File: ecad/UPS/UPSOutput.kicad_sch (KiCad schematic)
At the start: 28 parts, among them J3 USB_C_Receptacle_USB2.0_16P, Q3 IRLR7843TRPBF, SW3 SW_DPDT_x2, U2 MPQ5031GRE-0001-AEC1-P, U3 L78L05_SOT89

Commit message: Output section of PCB
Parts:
- C10, C11, C12, C60: footprint (none) -> Capacitor_SMD:C_0805_2012Metric_Pad1.18x1.45mm_HandSolder
- C5, C59, C6, C7, C8, C9: footprint (none) -> Capacitor_SMD:C_0603_1608Metric_Pad1.08x0.95mm_HandSolder
- R6, R7: footprint (none) -> Resistor_SMD:R_1206_3216Metric_Pad1.30x1.75mm_HandSolder
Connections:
- net CC1: now also D1.1 (K), J3.A5 (CC1), R7.1; no longer D2.1 (K), J3.B5 (CC2), R6.2
- net CC2: now also D2.1 (K), J3.B5 (CC2), R6.2; no longer D1.1 (K), J3.A5 (CC1), R7.1
- net VBUS renamed VBUS_out
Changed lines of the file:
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@@
 		)
 	)
-	(label "CC2"
-		(at 217.17 64.77 0)
+	(label "D+"
+		(at 217.17 52.07 0)
 		(effects
 			(font
@@
 		)
 	)
-	(label "CC1"
-		(at 217.17 62.23 0)
+	(label "VBUS_in"
+		(at 39.37 102.87 0)
 		(effects
 			(font
@@
 		)
 	)
-	(label "D+"
-		(at 217.17 52.07 0)
+	(label "SCL"
+		(at 29.21 62.23 0)
 		(effects
 			(font
@@
 		)
 	)
-	(label "SCL"
-		(at 29.21 62.23 0)
+	(label "D-"
+		(at 217.17 54.61 0)
 		(effects
 			(font
@@
 		)
 	)
-	(label "D-"
-		(at 217.17 54.61 0)
+	(label "VBUS_out"
+		(at 217.17 102.87 0)
 		(effects
 			(font
@@
 		)
 	)
-	(label "VBUS"
-		(at 217.17 102.87 0)
+	(label "CC1"
+		(at 217.17 64.77 0)
+		(effects
+			(font
+				(size 1.27 1.27)
+			)
+			(justify left bottom)
+		)
+	)
+	(label "CC2"
+		(at 217.17 62.23 0)
 		(effects
 			(font
@@
 			)
 		)
-		(property "Footprint" ""
+		(property "Footprint" "Capacitor_SMD:C_0603_1608Metric_Pad1.08x0.95mm_HandSolder"
 			(at 204.1652 78.74 0)
 			(effects
@@
 			)
 		)
-		(property "Footprint" ""
+		(property "Footprint" "Resistor_SMD:R_1206_3216Metric_Pad1.30x1.75mm_HandSolder"
 			(at 143.51 46.482 90)
 			(effects
@@
 			)
 		)
-		(property "Footprint" ""
+		(property "Footprint" "Resistor_SMD:R_1206_3216Metric_Pad1.30x1.75mm_HandSolder"
 			(at 143.51 47.498 90)
 			(effects
@@
 			)
 		)
-		(property "Footprint" ""
+		(property "Footprint" "Capacitor_SMD:C_0603_1608Metric_Pad1.08x0.95mm_HandSolder"
 			(at 30.1752 115.57 0)
 			(effects
@@
 			)
 		)
-		(property "Footprint" ""
+		(property "Footprint" "Capacitor_SMD:C_0603_1608Metric_Pad1.08x0.95mm_HandSolder"
 			(at 65.7352 78.74 0)
 			(effects
@@
 			)
 		)
-		(property "Footprint" ""
+		(property "Footprint" "Capacitor_SMD:C_0603_1608Metric_Pad1.08x0.95mm_HandSolder"
 			(at 130.5052 73.66 0)
 			(effects
@@
 			)
 		)
-		(property "Footprint" ""
+		(property "Footprint" "Capacitor_SMD:C_0805_2012Metric_Pad1.18x1.45mm_HandSolder"
 			(at 56.1848 78.74 0)
 			(effects
@@
 			)
 		)
-		(property "Footprint" ""
+		(property "Footprint" "Capacitor_SMD:C_0805_2012Metric_Pad1.18x1.45mm_HandSolder"
 			(at 143.51 81.5848 0)
 			(effects
@@
 			)
 		)
-		(property "Footprint" ""
+		(property "Footprint" "Capacitor_SMD:C_0603_1608Metric_Pad1.08x0.95mm_HandSolder"
 			(at 135.5852 73.66 0)
 			(effects
@@
 			)
 		)
-		(property "Footprint" ""
+		(property "Footprint" "Capacitor_SMD:C_0603_1608Metric_Pad1.08x0.95mm_HandSolder"
 			(at 176.8348 78.74 0)
 			(effects
@@
 			)
 		)
-		(property "Footprint" ""
+		(property "Footprint" "Capacitor_SMD:C_0805_2012Metric_Pad1.18x1.45mm_HandSolder"
 			(at 30.1752 128.27 0)
 			(effects
@@
 			)
 		)
-		(property "Footprint" ""
+		(property "Footprint" "Capacitor_SMD:C_0805_2012Metric_Pad1.18x1.45mm_HandSolder"
 			(at 234.95 84.1248 0)
 			(effects

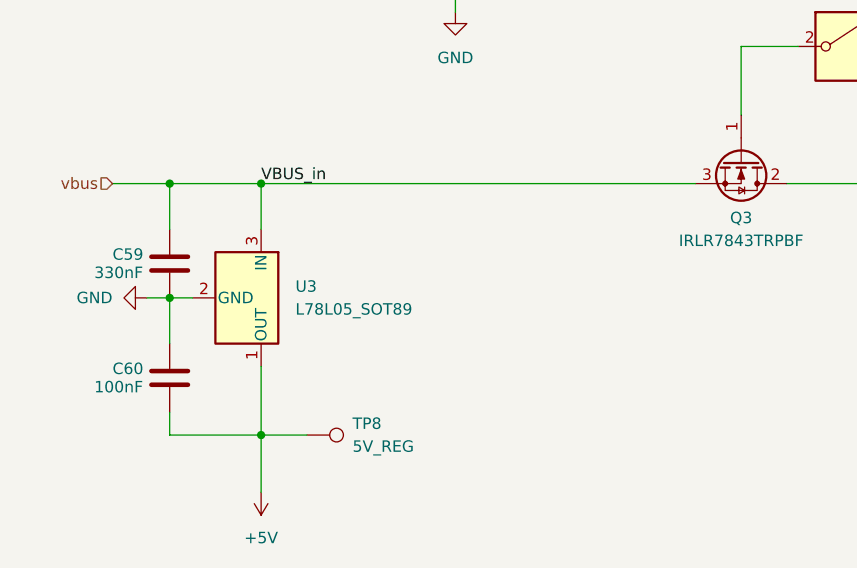
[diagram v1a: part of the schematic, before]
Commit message: Introduce fuses and a bit more routing
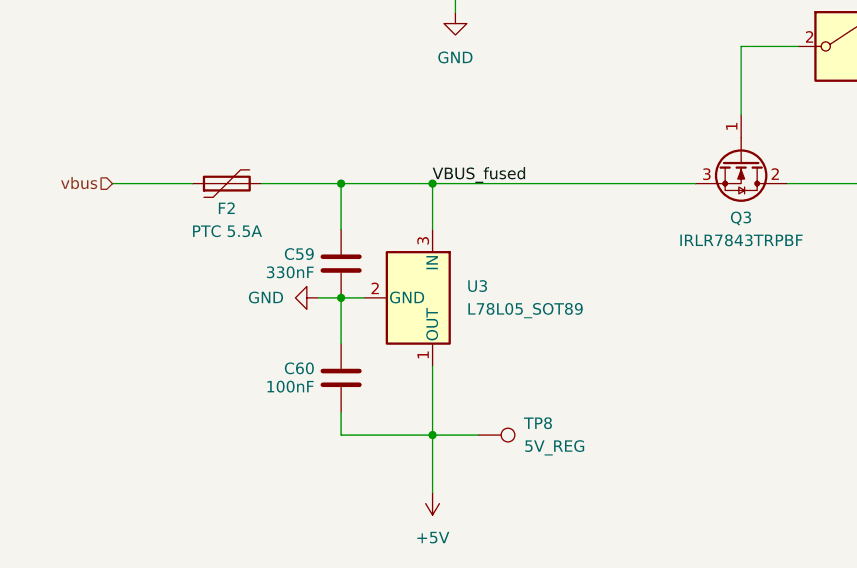
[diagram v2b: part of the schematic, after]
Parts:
- added F2: PTC 5.5A, Fuse:Fuse_1210_3225Metric_Pad1.42x2.65mm_HandSolder, symbol Device:Polyfuse
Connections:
- net vbus: now also F2.1; no longer C59.1, Q3.3 (S), U3.3 (IN)
- new net VBUS_fused: C59.1, F2.2, Q3.3 (S), U3.3 (IN)
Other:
- moved on the sheet: C59, C60, TP8, U3

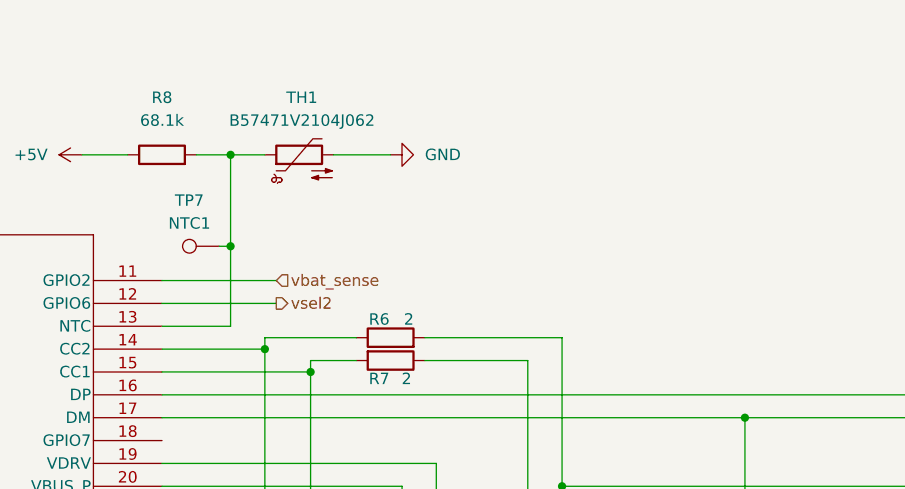
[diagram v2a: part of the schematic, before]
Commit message: VBATSENSE divider put in and some routing
Little more routing, complete by tonight
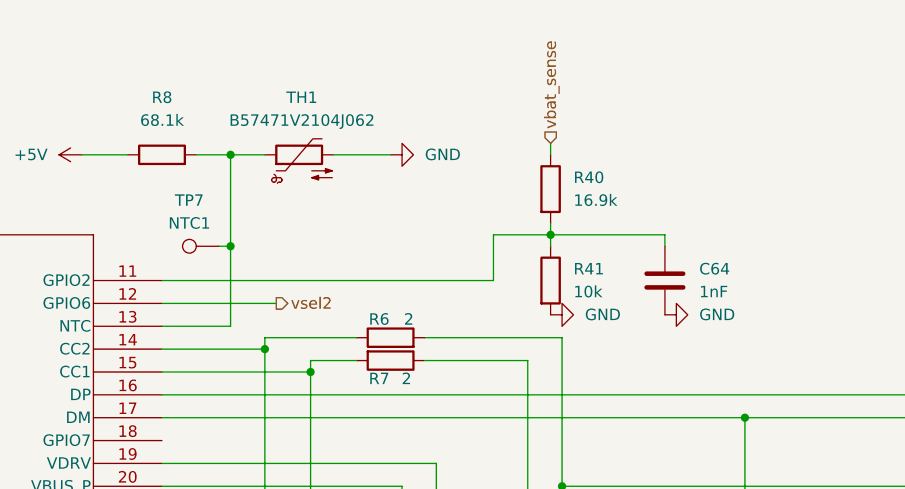
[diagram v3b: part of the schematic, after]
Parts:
- added C64: 1nF, symbol Device:C
- added R40: 16.9k, Resistor_SMD:R_0201_0603Metric_Pad0.64x0.40mm_HandSolder, symbol Device:R
- added R41: 10k, Resistor_SMD:R_0201_0603Metric_Pad0.64x0.40mm_HandSolder, symbol Device:R
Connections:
- net GND: now also C64.2, R41.2
- net vbat_sense: now also R40.1; no longer U2.11 (GPIO2)
- new net: C64.1, R40.2, R41.1, U2.11 (GPIO2)
